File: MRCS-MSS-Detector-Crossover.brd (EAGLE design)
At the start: 50 x 50 mm, 15 parts, among them J1 RJ45, J2 RJ45, X1 TRACK, X2 AUXBUS, X3 BLK OCC, X4 0.156/5

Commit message: fix commas in xml
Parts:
- C1, C2: device cap-pan:E2,5-6 -> cap-pan:E2.5-6
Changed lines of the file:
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@@
 <attribute name="VALUE" x="30.0228" y="32.1056" size="1.27" layer="51" ratio="10"/>
 </element>
-<element name="C1" library="cap-pan" package="E2,5-6" value="47uf 25V" x="30.988" y="22.225" smashed="yes" rot="R90">
+<element name="C1" library="cap-pan" package="E2.5-6" value="47uf 25V" x="30.988" y="22.225" smashed="yes" rot="R90">
 <attribute name="NAME" x="33.782" y="20.32" size="1.27" layer="25" ratio="10" rot="R270"/>
 <attribute name="VALUE" x="26.67" y="16.51" size="1.016" layer="27" ratio="10" rot="R270"/>
 </element>
-<element name="C2" library="cap-pan" package="E2,5-6" value="0.47uf 63V" x="11.43" y="22.225" smashed="yes" rot="R90">
+<element name="C2" library="cap-pan" package="E2.5-6" value="0.47uf 63V" x="11.43" y="22.225" smashed="yes" rot="R90">
 <attribute name="NAME" x="14.605" y="20.32" size="1.27" layer="25" ratio="10" rot="R270"/>
 <attribute name="VALUE" x="10.16" y="16.51" size="1.016" layer="27" ratio="10" rot="R270"/>

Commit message: fix commas in xml
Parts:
- U$3, U$4, U$5, U$6: device holes:3,6 -> holes:3.6
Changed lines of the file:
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@@
 <attribute name="VALUE" x="22.86" y="16.51" size="1.016" layer="27" ratio="10" rot="R270"/>
 </element>
-<element name="U$3" library="holes" package="3,6" value="" x="5.08" y="43.18" smashed="yes"/>
-<element name="U$4" library="holes" package="3,6" value="" x="5.08" y="5.08" smashed="yes"/>
-<element name="U$5" library="holes" package="3,6" value="" x="45.72" y="5.08" smashed="yes"/>
-<element name="U$6" library="holes" package="3,6" value="" x="45.72" y="43.815" smashed="yes"/>
+<element name="U$3" library="holes" package="3.6" value="" x="5.08" y="43.18" smashed="yes"/>
+<element name="U$4" library="holes" package="3.6" value="" x="5.08" y="5.08" smashed="yes"/>
+<element name="U$5" library="holes" package="3.6" value="" x="45.72" y="5.08" smashed="yes"/>
+<element name="U$6" library="holes" package="3.6" value="" x="45.72" y="43.815" smashed="yes"/>
 <element name="BOARD1" library="SPCoast" package="BOARD-SEEED5X5-NOHOLES" value="SEEED Fusion" x="0" y="0"/>
 </elements>

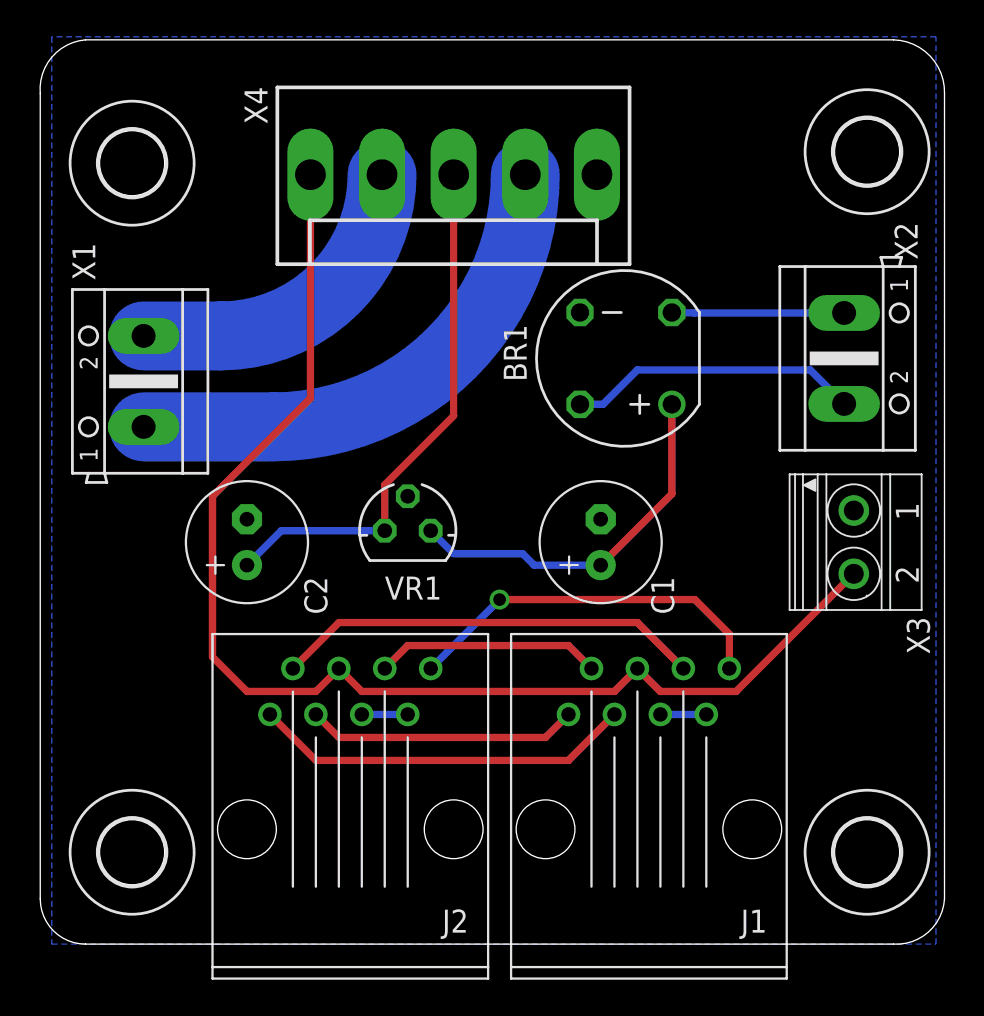
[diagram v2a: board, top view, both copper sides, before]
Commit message: Moved all components into SPCoast.lbr and panelized
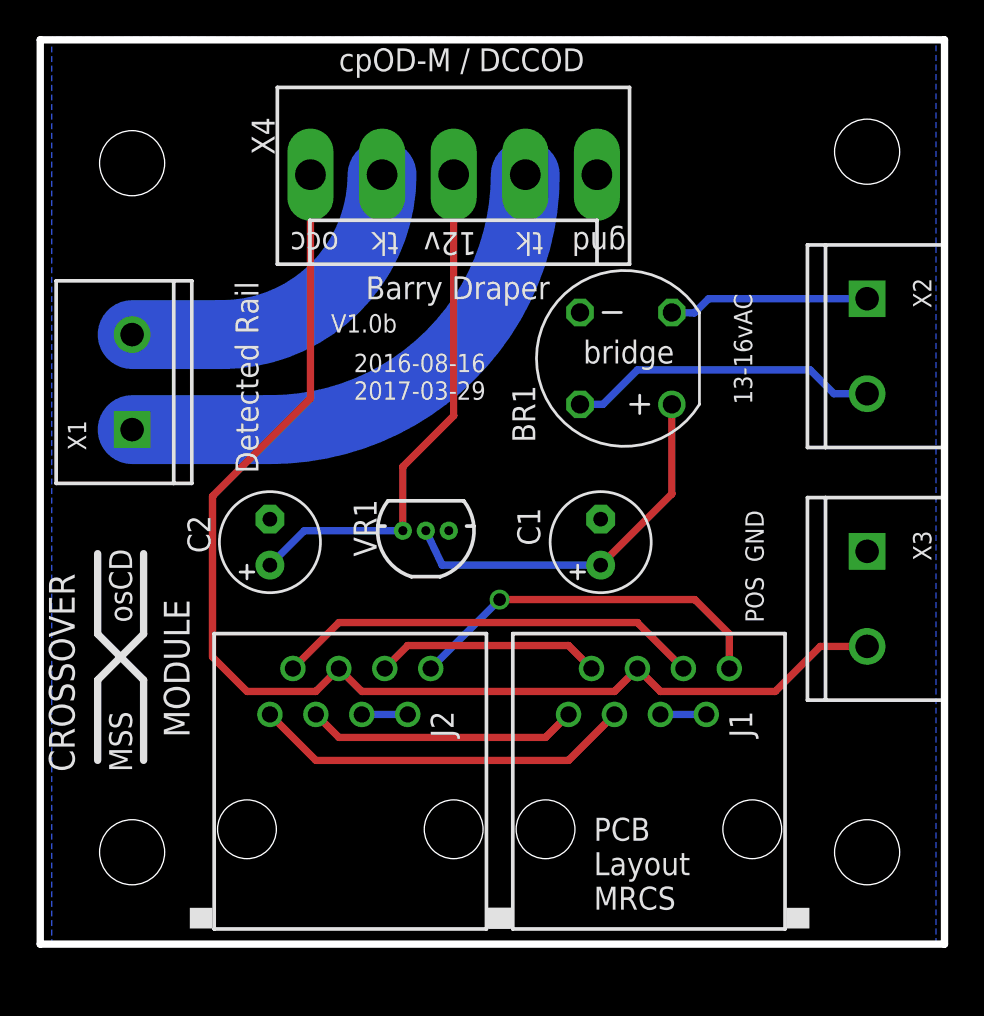
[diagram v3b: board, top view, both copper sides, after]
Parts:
- removed BOARD1: SEEED Fusion, SPCoast:BOARD-SEEED5X5-NOHOLES
- removed U$3, U$4, U$5, U$6: (no value), holes:3.6
- BR1: device rectifier:RB1A -> SPCoast:RB1A
- C1, C2: device cap-pan:E2.5-6 -> SPCoast:E2.5-6
- J1, J2: value RJ45 -> (none); device con-rj:RJ45 -> SPCoast:RJ45-NO-SHIELD
- VR1: device v-reg:78LXX -> SPCoast:TO-92
- X1, X2: device con-ptr500:AK500/2 -> SPCoast:SCREWTERMINAL-5MM-2
- X3: value BLK OCC -> BLOCKOCC; device con-phoenix-350:1751248 -> SPCoast:SCREWTERMINAL-5MM-2
- X4: value 0.156/5 -> (none); device con-molex:KK-156-5 -> SPCoast:KK-156-5
- moved X2 3.42 mm to (45.7, 35.6)
- moved X1 2.62 mm to (5.08, 28.6)
- moved C2 1.27 mm to (12.7, 22.2)
- moved VR1 1.00 mm to (21.3, 22.9), turned to 180 degrees
- moved X3 0.90 mm to (45.7, 21.6)
- turned J1 to 0 degrees
- turned J2 to 0 degrees
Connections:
- net GND: now also VR1.1; no longer VR1.GND
- net V12: now also VR1.3; no longer VR1.OUT
- net VIN: now also VR1.2; no longer VR1.IN
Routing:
- net AC2: track 9.53 -> 11.1 mm
- net AC1: track 16.2 -> 17.2 mm
- net N$10: track 70.0 -> 69.0 mm
- net TRACK1: track 26.9 -> 27.6 mm
- net VIN: track 20.7 -> 21.4 mm
- net V12: track 29.7 -> 29.0 mm
- net TRACK2: track 16.9 -> 17.5 mm
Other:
- outline, holes or cut-outs redrawn
- board text added: "BR1"
- board text added: "C1"
- board text added: "C2"
- board text added: "J1"
- board text added: "J2"
- board text added: "PCB Layout MRCS"
- board text added: "TRACK"
- board text added: "VR1"
- board text added: "X1"
- board text added: "X2"
- board text added: "X3"
- board text added: "X4"
- board text removed: "PCB Layout SCN & JMP"
